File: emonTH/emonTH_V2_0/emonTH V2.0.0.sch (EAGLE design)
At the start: 47 parts, among them J1 1X2-3.5MM, J2 1X2-3.5MM, J3 1X2-3.5MM, Q1 16Mhz, Q2 DS18B20, U1 LTC3525ESC6-3.3TRMPBF, U1_MLF ATMEGA168MLF, U1_TQFP ATMEGA328P, U2 SI7021

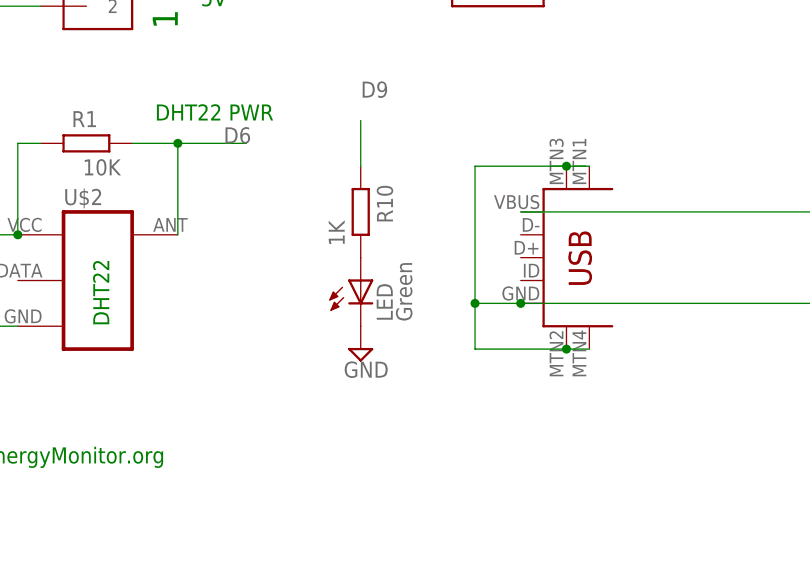
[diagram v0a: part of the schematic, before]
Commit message: add emonth v2.0.1 led footprint update
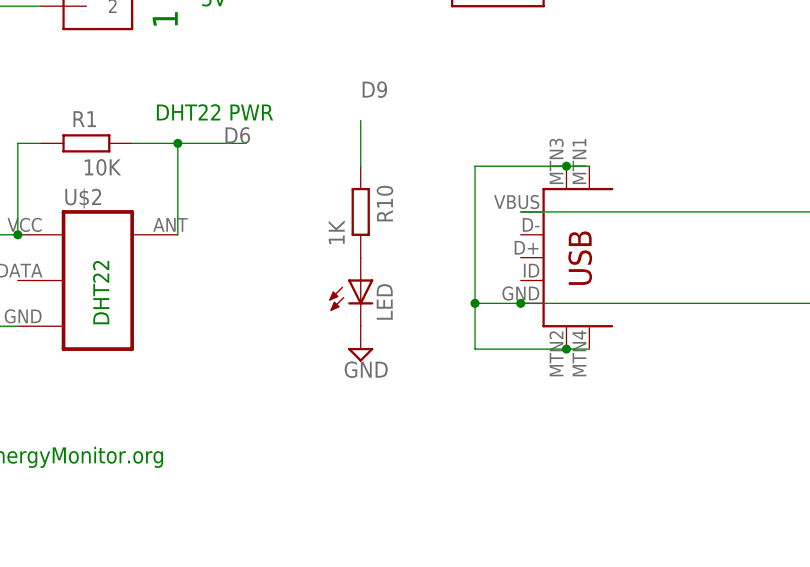
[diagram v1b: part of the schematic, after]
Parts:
- LED: value Green -> (none); device adafruit:LEDCHIP-LED0805 -> adafruit:LEDCHIPLED-0603-TTW
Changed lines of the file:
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@@
 <?xml version="1.0" encoding="utf-8"?>
 <!DOCTYPE eagle SYSTEM "eagle.dtd">
-<eagle version="7.5.0">
+<eagle version="7.6.0">
 <drawing>
 <settings>
@@
 </classes>
 <parts>
-<part name="LED" library="adafruit" deviceset="LED" device="CHIP-LED0805" value="Green"/>
 <part name="R10" library="resistor" deviceset="R-EU_" device="R0603" value="1K"/>
 <part name="SUPPLY25" library="supply2" deviceset="GND" device=""/>
@@
 <part name="SUPPLY1" library="supply2" deviceset="GND" device=""/>
 <part name="+3V1" library="supply1" deviceset="+3V3" device=""/>
+<part name="LED" library="adafruit" deviceset="LED" device="CHIPLED-0603-TTW"/>
 </parts>
 <sheets>
@@
 </plain>
 <instances>
-<instance part="LED" gate="G$1" x="58.42" y="223.52"/>
 <instance part="R10" gate="G$1" x="58.42" y="231.14" smashed="yes" rot="R90">
 <attribute name="NAME" x="62.0014" y="229.87" size="1.778" layer="95" rot="R90"/>
@@
 <instance part="SUPPLY1" gate="GND" x="114.3" y="264.16"/>
 <instance part="+3V1" gate="G$1" x="152.4" y="292.1"/>
+<instance part="LED" gate="G$1" x="58.42" y="223.52"/>
 </instances>
 <busses>
@@
 </net>
 <net name="GND" class="2">
-<segment>
-<pinref part="LED" gate="G$1" pin="C"/>
-<pinref part="SUPPLY25" gate="GND" pin="GND"/>
-</segment>
 <segment>
 <wire x1="-15.24" y1="218.44" x2="-15.24" y2="215.9" width="0.1524" layer="91"/>
@@
 <wire x1="104.14" y1="266.7" x2="114.3" y2="266.7" width="0.1524" layer="91"/>
 </segment>
-</net>
-<net name="N$41" class="0">
-<segment>
-<pinref part="R10" gate="G$1" pin="1"/>
-<pinref part="LED" gate="G$1" pin="A"/>
+<segment>
+<pinref part="SUPPLY25" gate="GND" pin="GND"/>
+<pinref part="LED" gate="G$1" pin="C"/>
 </segment>
 </net>
@@
 </segment>
 </net>
+<net name="N$1" class="0">
+<segment>
+<pinref part="R10" gate="G$1" pin="1"/>
+<pinref part="LED" gate="G$1" pin="A"/>
+</segment>
+</net>
